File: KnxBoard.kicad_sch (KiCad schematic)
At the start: 44 parts, among them IC1 STM32G491KEU6, IC2 NCN5130MNTWG, J1 Conn_01x02, J2 Conn_02x03_Counter_Clockwise, J3 Conn_01x10, J4 Conn_01x10, SW1 SW_Push, Y1 16MHz

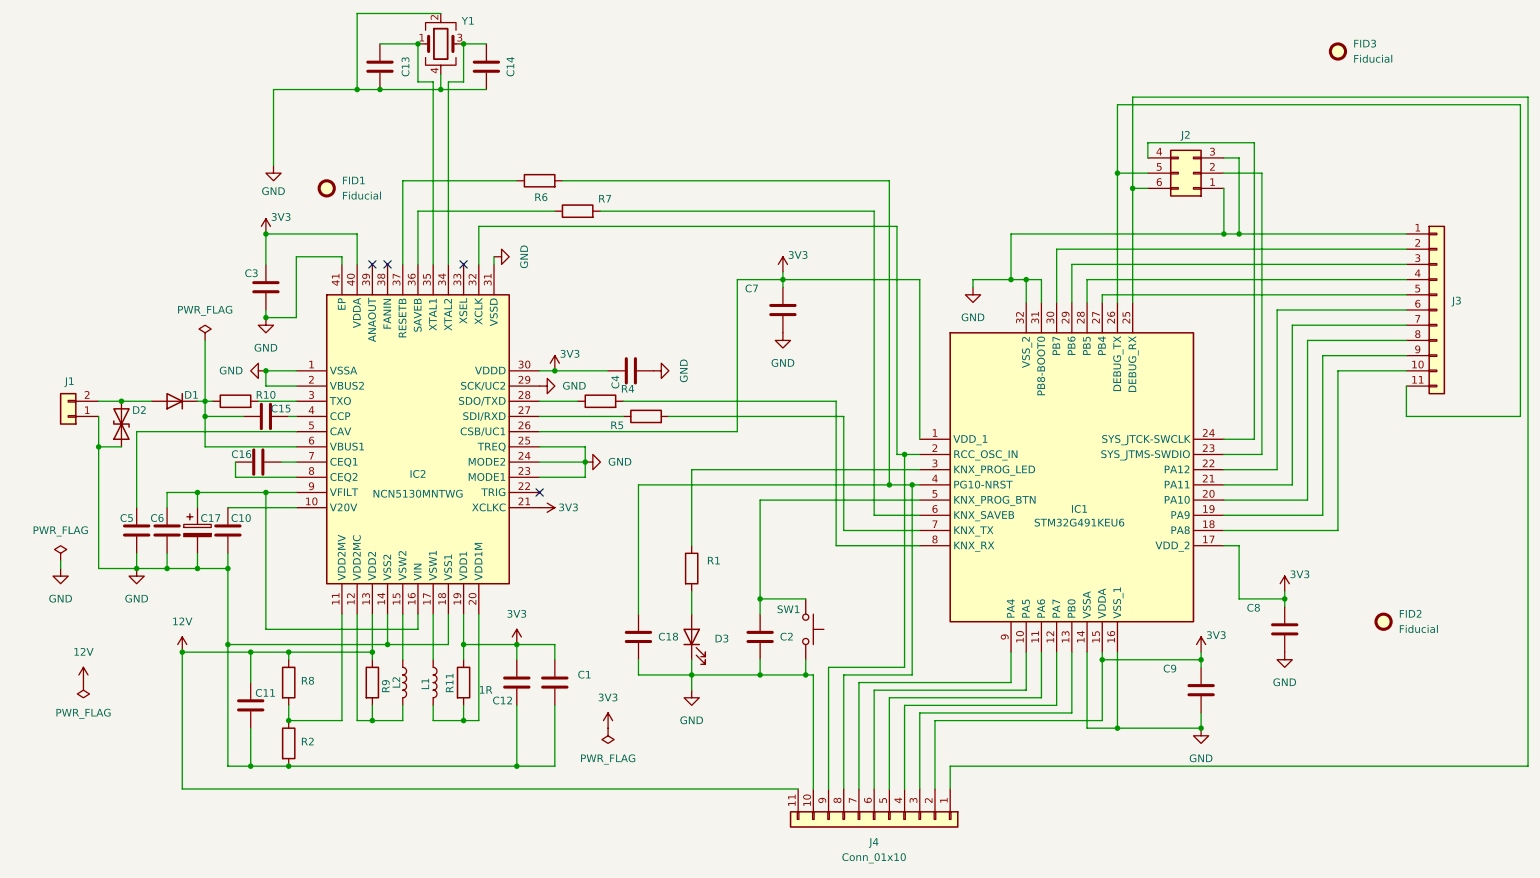
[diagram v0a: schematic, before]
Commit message: Add NRST and 3V3 to debug connector
Connect ANAOUT to STM ADC to be able to support the KNX System B standard

Update to kicad 10.0
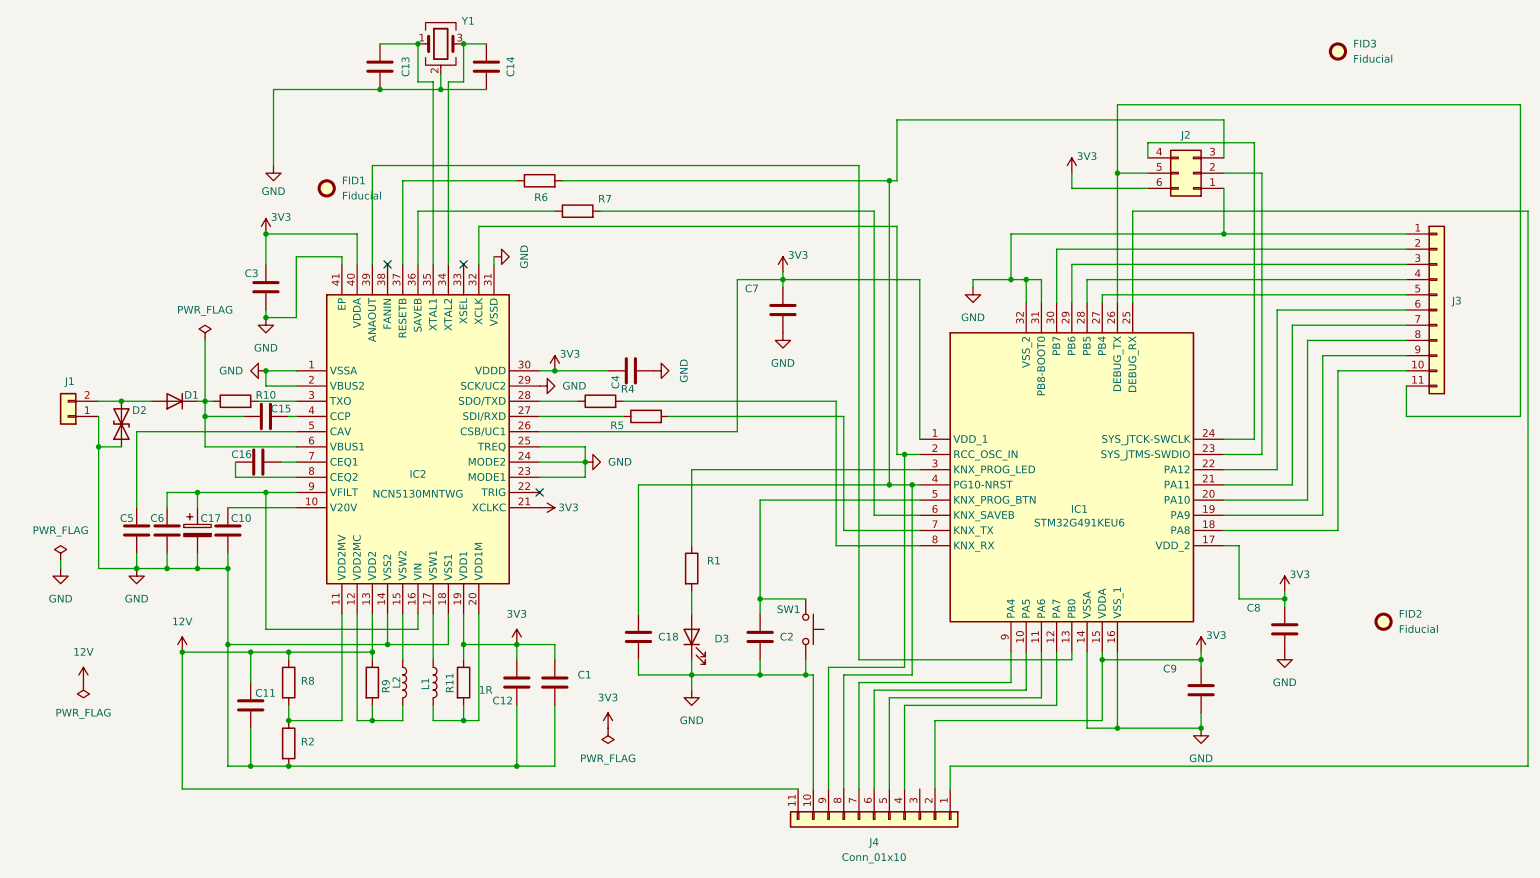
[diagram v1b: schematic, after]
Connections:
- net 3V3: now also J2.6 (Pin_6)
- net GND: no longer J2.3 (Pin_3)
- net at C18.1, IC1.4 (PG10-NRST), J4.8 (Pin_8)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: now also J2.3 (Pin_3)
- net at IC1.25 (DEBUG_RX), J4.1 (Pin_1): no longer J2.6 (Pin_6)
- net at J4.3 (Pin_3): no longer IC1.13 (PB0)
- net at IC2.39 (ANAOUT): now also IC1.13 (PB0)
- no-connect marks 4 -> 3

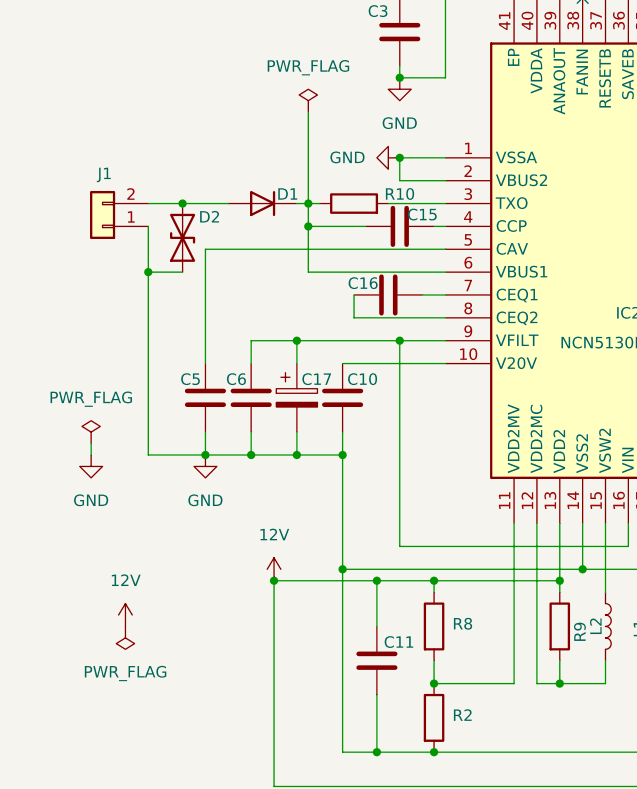
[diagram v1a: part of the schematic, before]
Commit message: Add new capa footprint on the other side
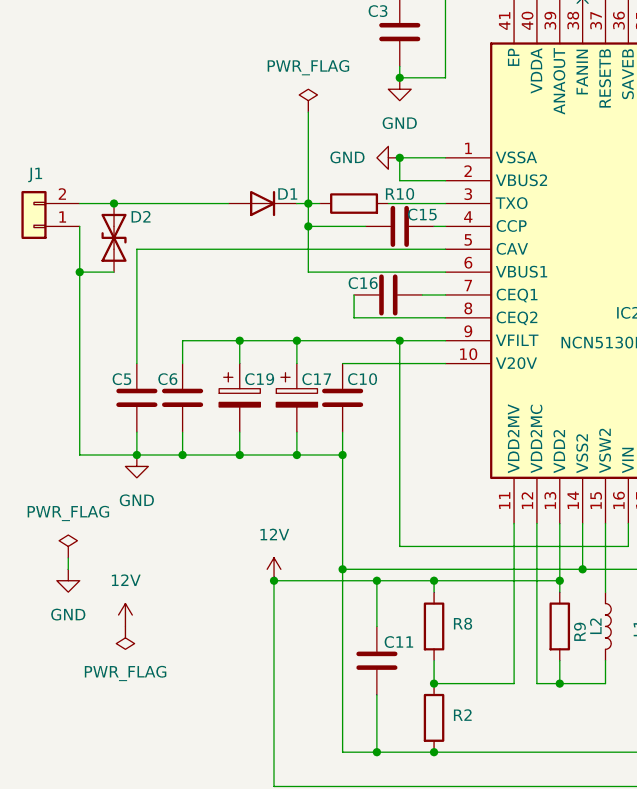
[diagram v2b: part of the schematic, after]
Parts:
- added C19: 100uF 35 Volt, Capacitor_SMD:CP_Elec_6.3x7.7, symbol Device:C_Polarized
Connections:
- net GND: now also C19.2
- net at C17.1, C6.1, IC2.16 (VIN)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: now also C19.1
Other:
- moved on the sheet: C5, C6, D2, J1
